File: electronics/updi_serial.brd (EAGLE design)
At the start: 27.9 x 13.2 mm, 11 parts, among them U1 CH340N

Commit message: update bottom silk
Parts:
- moved U$5 11.7 mm to (14.0, 6.60)
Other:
- board text added: "https://is.gd/8LZyVP"

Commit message: changed pin hdr package, updated silk
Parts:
- JP1: device pinhead-2:1X03/90-S -> pinhead-2:1X03-S
- moved JP1 3.81 mm to (26.0, 6.60)
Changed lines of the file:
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@@
 <wire x1="0" y1="13.208" x2="0" y2="0" width="0" layer="20"/>
 <text x="24.765" y="4.064" size="0.8128" layer="25" font="vector" ratio="10" align="center-right">UPDI</text>
-<text x="24.892" y="9.144" size="0.8128" layer="25" font="vector" ratio="10" align="center-right">VCC</text>
-<text x="24.892" y="6.604" size="0.8128" layer="25" font="vector" ratio="10" align="center-right">GND</text>
+<text x="24.765" y="9.144" size="0.8128" layer="25" font="vector" ratio="10" align="center-right">VCC</text>
+<text x="24.765" y="6.604" size="0.8128" layer="25" font="vector" ratio="10" align="center-right">GND</text>
 <text x="13.97" y="11.303" size="1.27" layer="26" font="vector" ratio="10" rot="MR0" align="bottom-center">UPDI Serial Programmer</text>
 <text x="13.97" y="3.556" size="1.27" layer="26" font="vector" ratio="10" rot="MR0" align="bottom-center">cc-by-sa</text>
@@
 <attribute name="NAME" x="15.748" y="10.922" size="0.8128" layer="25" font="vector" rot="R180" align="bottom-center"/>
 </element>
-<element name="JP1" library="pinhead-2" package="1X03/90-S" value="" x="29.845" y="6.604" smashed="yes" rot="R270">
-<attribute name="VALUE" x="26.035" y="0.889" size="1.27" layer="27"/>
-</element>
-<element name="JP2" library="bt_electromech" package="USB-MINIB" value="USB-MINIB" x="5.08" y="6.604">
+<element name="JP1" library="pinhead-2" package="1X03-S" value="" x="26.035" y="6.604" smashed="yes" rot="R270">
+<attribute name="VALUE" x="22.225" y="0.889" size="1.27" layer="27"/>
+</element>
+<element name="JP2" library="bt_electromech" package="USB-MINIB" value="USB-MINIB" x="5.08" y="6.604" smashed="yes">
 <attribute name="PROD_ID" value="CONN-08193" x="5.08" y="6.604" size="1.778" layer="27" display="off"/>
 </element>

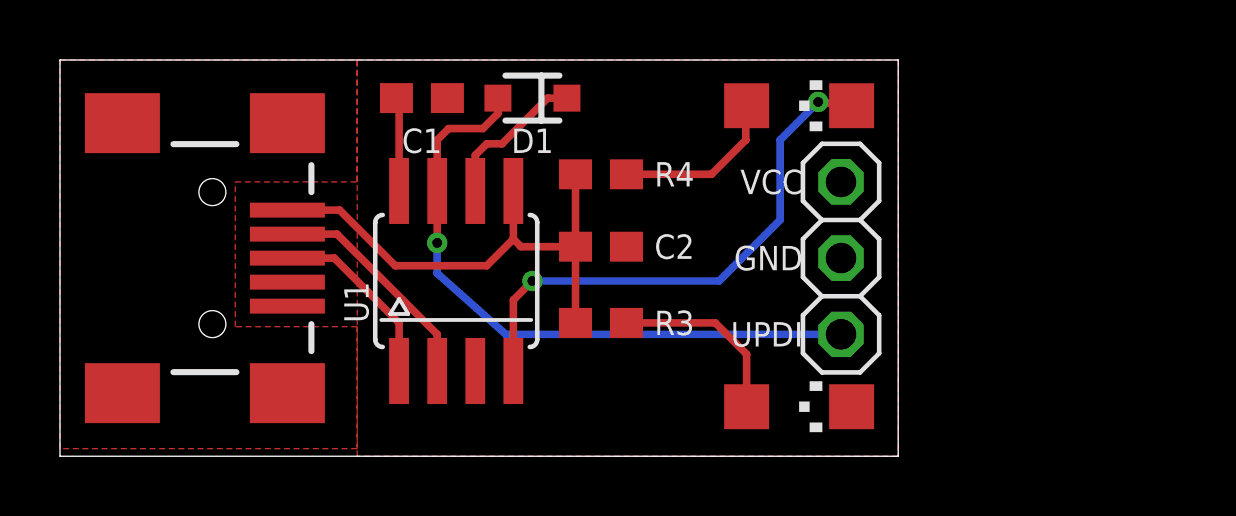
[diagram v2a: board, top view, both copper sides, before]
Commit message: replaced solder jmpr with pin hdr, layout changes, pwr led indicates target pwr now
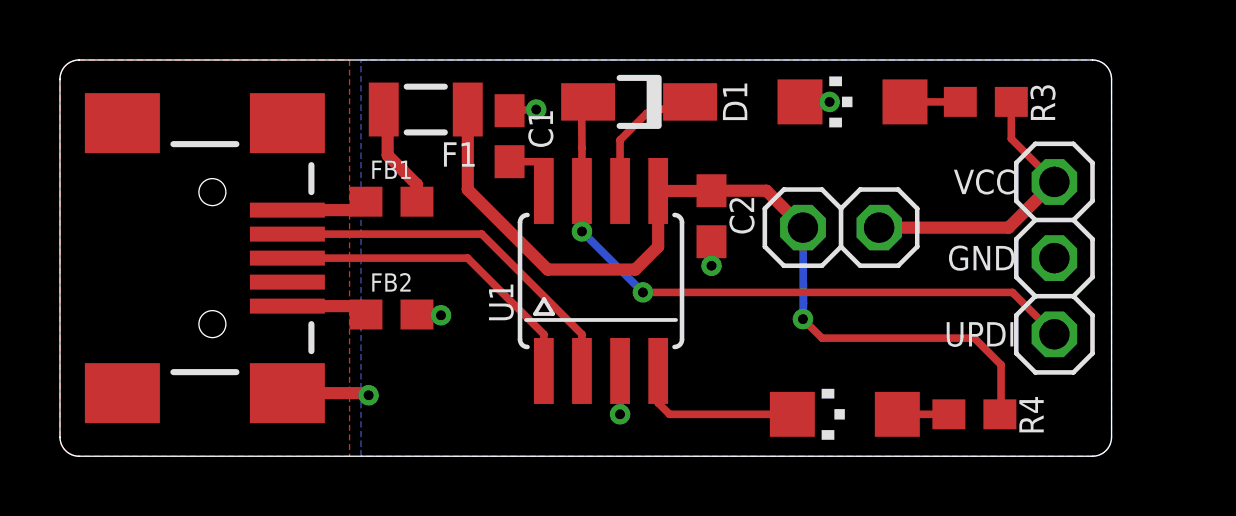
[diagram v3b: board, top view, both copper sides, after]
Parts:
- added F1: PTCSMD, bt:PTC-1206
- added FB1, FB2: 1kΩ@100MHz/200mΩ/1A, SparkFun-Coils:0603
- added JP3: VBUS>VCC, bt:JUMPER-PIN-0.1IN
- D1: device bt_diode:SOD-323 -> bt_diode:SOD123FL
- LED1: value PWR -> VCC(TGT)
- LED2: value PRG -> PROG
- moved R4 14.8 mm to (30.5, 1.40), turned to 180 degrees
- moved R3 14.8 mm to (30.9, 11.8), turned to 180 degrees
- moved LED2 10.4 mm to (26.2, 1.40), turned to 180 degrees
- moved LED1 10.3 mm to (26.4, 11.8), turned to 180 degrees
- moved JP1 7.11 mm to (33.1, 6.60)
- moved U$5 4.83 mm to (18.8, 6.60)
- moved U1 4.83 mm to (18.0, 5.84)
- moved C2 3.82 mm to (21.7, 8.00), turned to 270 degrees
- moved D1 3.56 mm to (19.3, 11.8)
- moved C1 3.19 mm to (15.0, 10.7), turned to 90 degrees
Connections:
- removed net SHIELD: JP2.MTN1, JP2.MTN2, JP2.MTN3, JP2.MTN4
- new net N$1: FB1.1, JP2.VBUS
- new net N$2: F1.1, FB1.2
- new net N$7: FB2.1, JP2.GND
- net GND: now also FB2.2, JP2.MTN1, JP2.MTN2, JP2.MTN3, JP2.MTN4; no longer JP2.GND
- net VCC: now also JP3.2, R3.1
- net VIN: now also F1.2, JP3.1; no longer JP2.VBUS, R3.1
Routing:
- net VIN: track 17.4 -> 30.0 mm, vias 0 -> 1
- net N$4: track 17.9 -> 5.69 mm, vias 2 -> 0
- net VCC: track 0.00 -> 9.74 mm
- net GND: track 0.00 -> 7.65 mm, vias 0 -> 6
- net DM: track 7.60 -> 12.4 mm
- net DP: track 6.22 -> 10.8 mm
- net N$6: track 6.19 -> 1.84 mm
- net N$5: track 5.60 -> 1.72 mm
- net N$2: track 0.00 -> 3.51 mm
- net N$7: track 0.00 -> 2.71 mm
- net N$1: track 0.00 -> 2.69 mm
- net N$8: track 3.11 -> 2.12 mm
- net N$3: track 5.04 -> 4.45 mm
- net UPDI: track 21.6 -> 21.5 mm, vias 1 -> 2
- added copper zone on layer 16, net GND
- removed copper zone on layer 1, net SHIELD
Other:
- board size 27.9 x 13.2 mm -> 35.1 x 13.2 mm
